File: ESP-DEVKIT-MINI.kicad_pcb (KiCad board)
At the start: 2 copper layers, 25.4 x 68.6 mm, 45 parts, among them J1 Conn_01x22_Pin, J2 Conn_01x22_Pin, J3 USB_C_Receptacle_USB2.0, J4 USB_B_Mini, J5 USB_B_Micro, Q1 L8050QLT1G, Q2 L8050QLT1G, SW1 SW_Omron_B3FS, SW2 SW_Omron_B3FS, U1 ESP32-S3-MINI-1-N8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

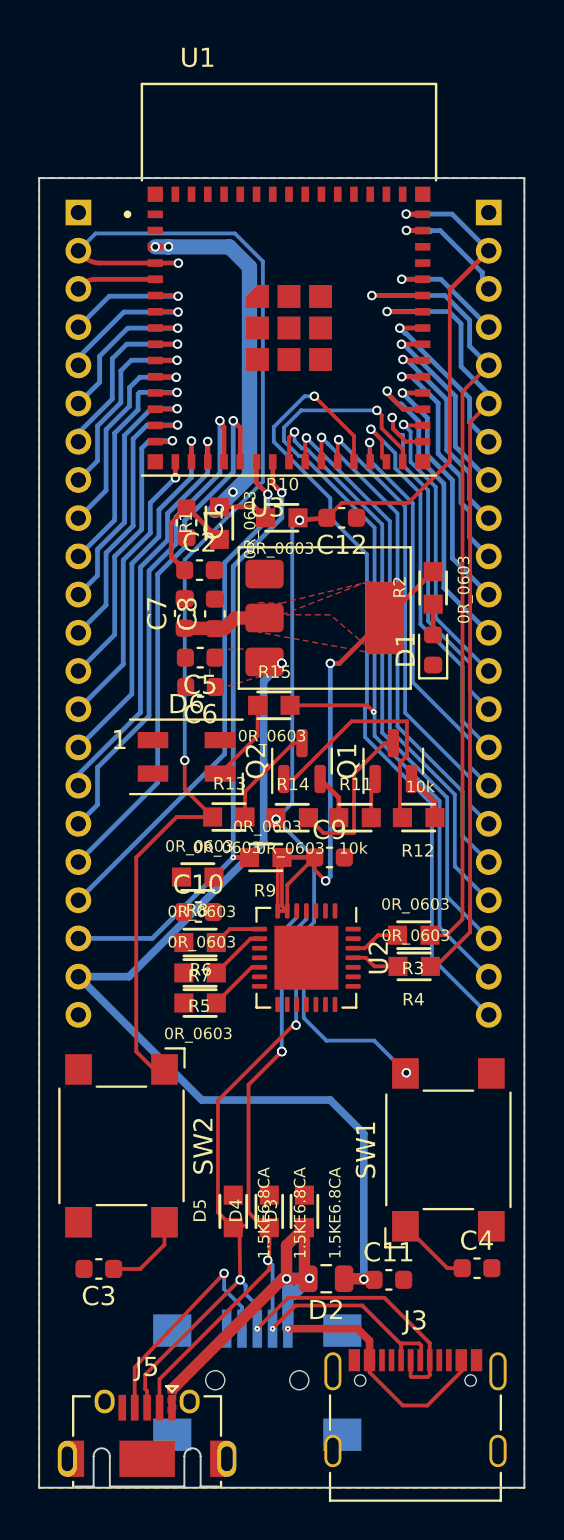
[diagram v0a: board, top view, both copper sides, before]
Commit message: Reorganizing the Silk screen
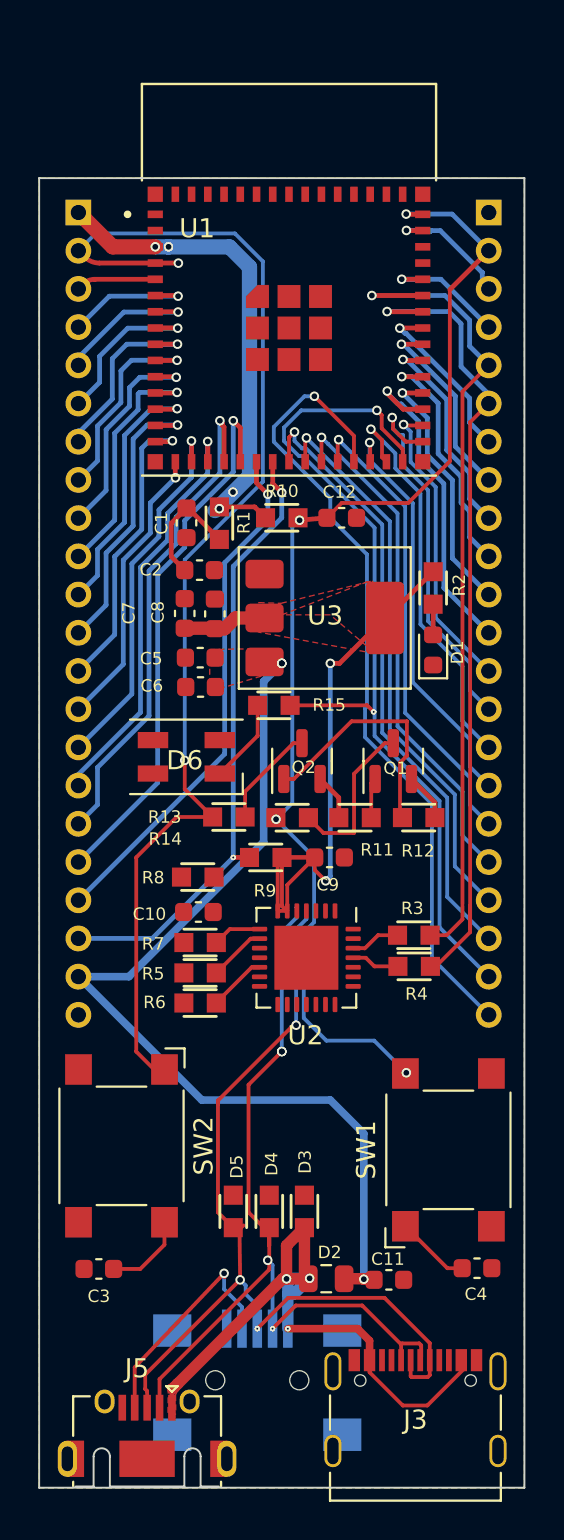
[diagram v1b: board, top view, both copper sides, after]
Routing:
- net ESP_3V3: track 21.5 -> 26.3 mm
- net VBUS: track 34.3 -> 35.3 mm
